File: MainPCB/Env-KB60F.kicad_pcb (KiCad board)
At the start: 2 copper layers, 283 x 126.5 mm, 143 parts, among them SW1 EVQ-P7A01P, U1 Pico

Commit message: Moved MCU lower to allow for mount hole to fit properly, Generated Gerber and bottom plate Gerber
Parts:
- moved 5.1K1 9.31 mm to (297.2, 37.0), turned to 180 degrees
- moved 5.1K2 5.92 mm to (297.2, 38.0), turned to 0 degrees
- moved U1 2.75 mm to (334.0, 51.8)
- moved H11 1.75 mm to (353.1, 36.5)
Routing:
- net col0: track 358.9 -> 350.4 mm
- net Net-(5.1K1-Pad1): track 1.71 -> 9.36 mm
- net col1: track 328.2 -> 320.6 mm
- net GND: track 10.6 -> 3.23 mm
- net VBUS: track 78.3 -> 85.7 mm, vias 0 -> 2
- net row0: track 245.8 -> 240.7 mm
- net col2: track 298.7 -> 293.9 mm
- net USB2_P: track 65.2 -> 69.8 mm, vias 1 -> 3
- net USB2_N: track 61.5 -> 66.1 mm, vias 1 -> 2
- net col14: track 142.9 -> 138.5 mm
- net Net-(5.1K2-Pad2): track 1.40 -> 5.80 mm
- net RUNPIN: track 39.0 -> 34.7 mm
- net col3: track 305.6 -> 301.9 mm
- net col5: track 251.1 -> 247.5 mm
- net col4: track 264.2 -> 260.6 mm
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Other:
- net class DIFF removed
- net class USB added: clearance 0.2, trace_width 0.25, via_dia 0.8, via_drill 0.4

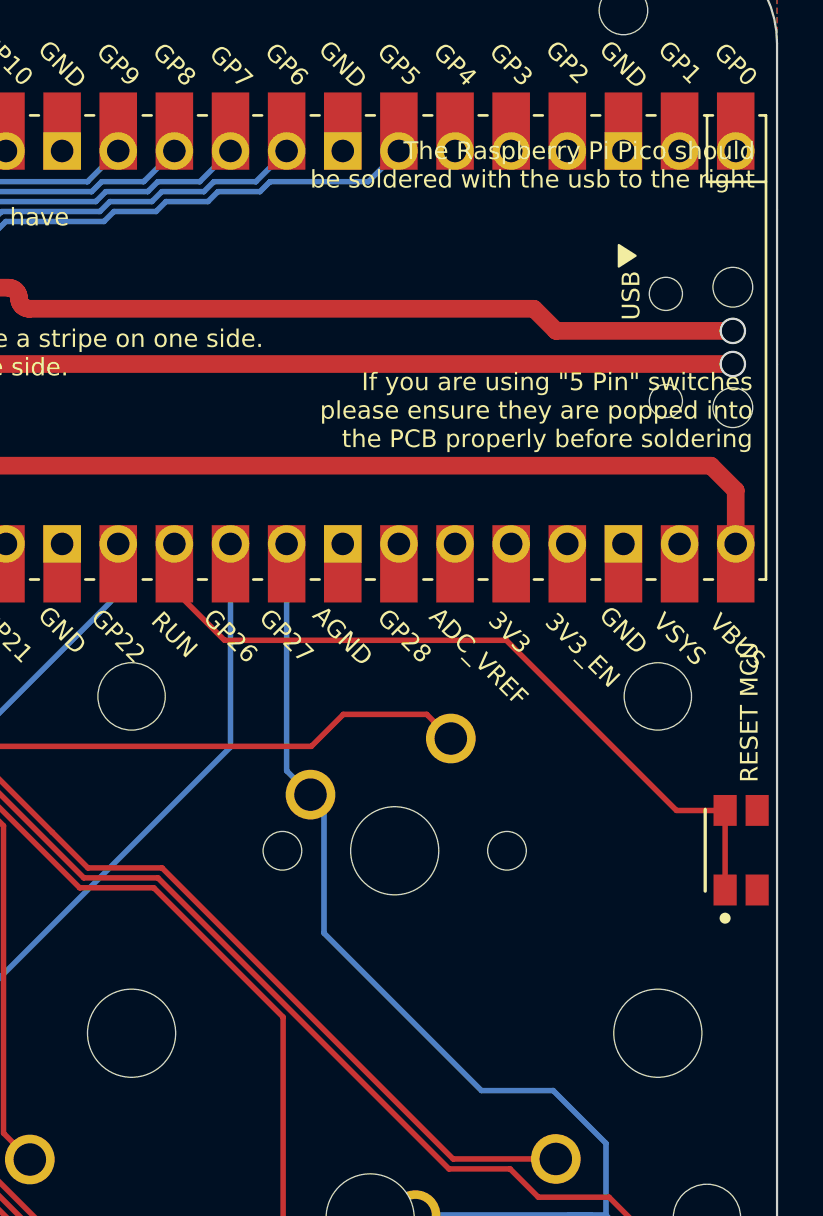
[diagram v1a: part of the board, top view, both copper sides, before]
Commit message: Corrected silkscreen, Generated updated Gerbers
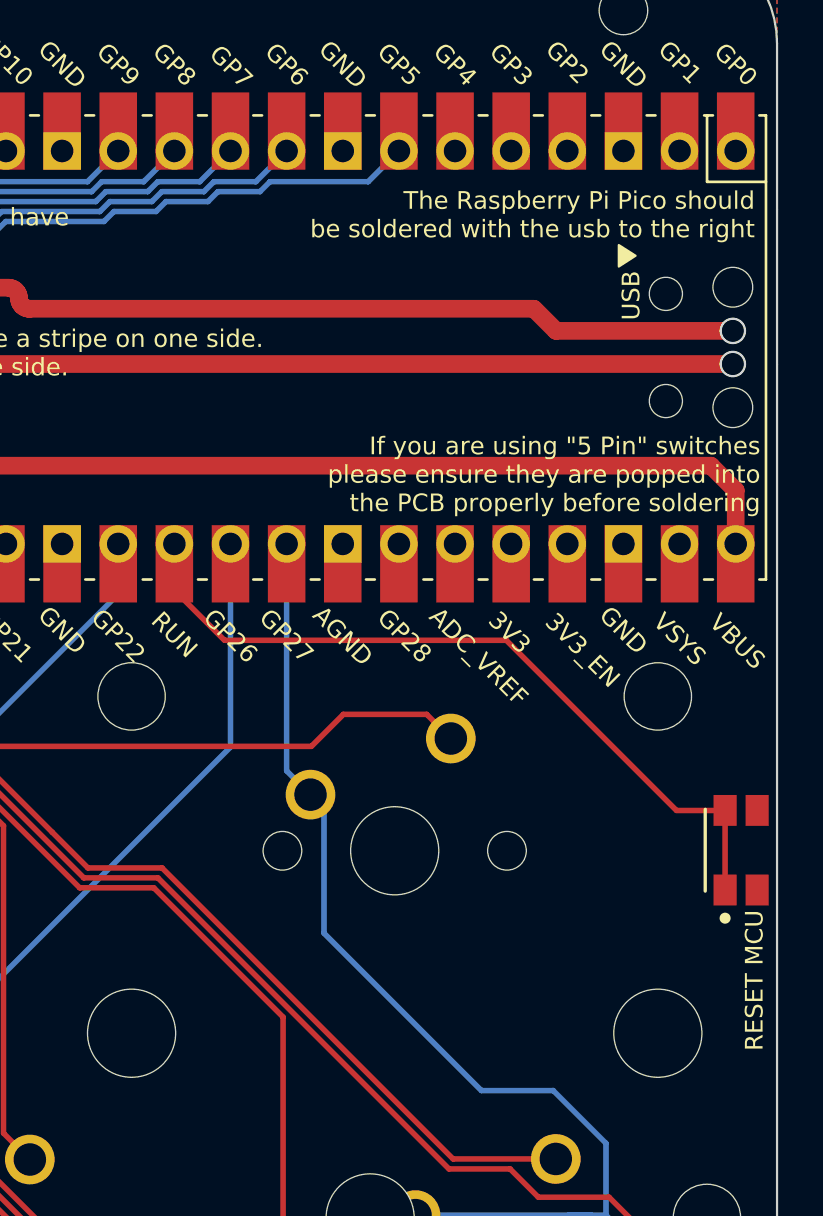
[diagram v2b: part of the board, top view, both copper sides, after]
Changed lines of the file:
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@@
     (pcbplotparams
       (layerselection 0x010fc_ffffffff)
-      (usegerberextensions false)
+      (usegerberextensions true)
       (usegerberattributes false)
       (usegerberadvancedattributes false)
@@
       (plotinvisibletext false)
       (padsonsilk false)
-      (subtractmaskfromsilk false)
+      (subtractmaskfromsilk true)
       (outputformat 1)
       (mirror false)
@@
     (effects (font (size 1 1) (thickness 0.15)) (justify mirror))
   )
-  (gr_text "RESET MCU" (at 358.75 68.25 90) (layer F.SilkS)
-    (effects (font (size 0.8 0.8) (thickness 0.153)))
+  (gr_text "RESET MCU" (at 358.975 77.2 90) (layer F.SilkS)
+    (effects (font (size 0.8 0.8) (thickness 0.153)) (justify right))
   )
   (gr_text Env-KB60F (at 85.9 56.5) (layer F.SilkS)
@@
     (effects (font (size 0.8 0.8) (thickness 0.15)))
   )
-  (gr_text "If you are using \"5 Pin\" switches\nplease ensure they are popped into\n the PCB properly before soldering" (at 358.9 54.6) (layer F.SilkS)
+  (gr_text "If you are using \"5 Pin\" switches\nplease ensure they are popped into\n the PCB properly before soldering" (at 359.25 57.5) (layer F.SilkS)
     (effects (font (size 0.8 0.8) (thickness 0.153)) (justify right))
   )
@@
     (effects (font (size 0.8 0.8) (thickness 0.153)) (justify left))
   )
-  (gr_text "The Raspberry Pi Pico should\nbe soldered with the usb to the right" (at 359 43.5) (layer F.SilkS)
+  (gr_text "The Raspberry Pi Pico should\nbe soldered with the usb to the right" (at 359 45.75) (layer F.SilkS)
     (effects (font (size 0.8 0.8) (thickness 0.153)) (justify right))
   )
@@
   (via (at 312.5 51.75) (size 0.8) (drill 0.4) (layers F.Cu B.Cu) (net 96))
   (via (at 306.3 62) (size 0.8) (drill 0.4) (layers F.Cu B.Cu) (net 96))
-  (via (at 300.75 42.6) (size 0.8) (drill 0.4) (layers F.Cu B.Cu) (net 100))
-  (via (at 358 51) (size 1.2) (drill 1) (layers F.Cu B.Cu) (net 103))
-  (via (at 358 52.5) (size 1.2) (drill 1) (layers F.Cu B.Cu) (net 104))
   (segment (start 357.65 76.3) (end 357.65 72.7) (width 0.25) (layer F.Cu) (net 97))
   (segment (start 347.75 65) (end 335 65) (width 0.25) (layer F.Cu) (net 97))
@@
   (segment (start 289.7 43.3) (end 291.38 43.3) (width 0.25) (layer F.Cu) (net 99))
   (segment (start 287.2 45.8) (end 289.7 43.3) (width 0.25) (layer F.Cu) (net 99))
+  (via (at 300.75 42.6) (size 0.8) (drill 0.4) (layers F.Cu B.Cu) (net 100))
   (via (at 307.3 43.25) (size 0.8) (drill 0.4) (layers F.Cu B.Cu) (net 100))
   (segment (start 305.445001 41.625001) (end 307.07 43.25) (width 0.5) (layer F.Cu) (net 100))
@@
   (segment (start 304.245001 38.645001) (end 302.6 37) (width 0.25) (layer F.Cu) (net 102))
   (segment (start 304.245001 40.650001) (end 304.245001 38.645001) (width 0.25) (layer F.Cu) (net 102))
+  (via (at 358 51) (size 1.2) (drill 1) (layers F.Cu B.Cu) (net 103))
   (segment (start 302.745001 41.995001) (end 303.75 43) (width 0.25) (layer F.Cu) (net 103))
   (segment (start 302.745001 40.650001) (end 302.745001 41.995001) (width 0.25) (layer F.Cu) (net 103))
@@
   (segment (start 323.972821 50.774173) (end 324.029633 50.683758) (width 0.8) (layer F.Cu) (net 103))
   (segment (start 324.076857 50.476857) (end 324.076857 50) (width 0.8) (layer F.Cu) (net 103))
+  (via (at 358 52.5) (size 1.2) (drill 1) (layers F.Cu B.Cu) (net 104))
   (segment (start 303.245001 39.177501) (end 303.245001 40.650001) (width 0.25) (layer F.Cu) (net 104))
   (segment (start 302.7675 38.7) (end 303.245001 39.177501) (width 0.25) (layer F.Cu) (net 104))

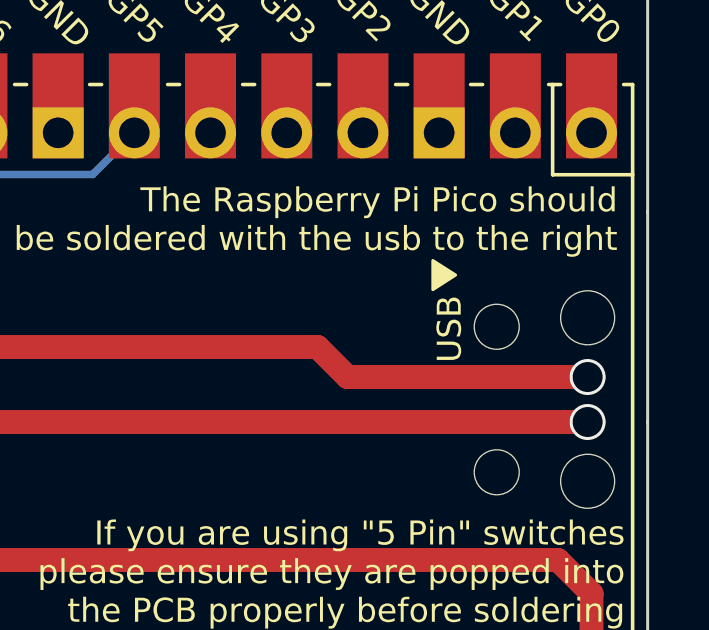
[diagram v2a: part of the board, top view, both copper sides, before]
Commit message: somehow missed a screwup on the silkscreen
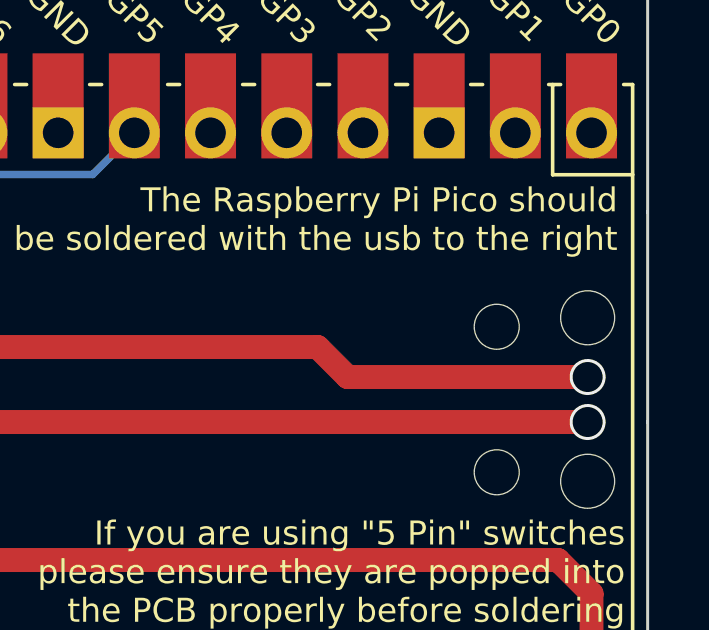
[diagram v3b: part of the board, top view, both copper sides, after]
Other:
- board text removed: "USB"

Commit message: General Checkover and adjustments, Generated Gerbers for JLCPCB
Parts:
- added J1: TP3 Pad, TestPoint:TestPoint_Pad_1.0x1.0mm, F.Cu at (358.0, 51.0)
- added J2: TP2 Pad, TestPoint:TestPoint_Pad_1.0x1.0mm, F.Cu at (358.0, 52.6)
- 5.1K1, 5.1K2: value R_Small -> 5.1K 0402 Resistor; footprint Resistor_SMD:R_0201_0603Metric -> Resistor_SMD:R_0402_1005Metric
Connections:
- USB1 pad 3: (no net) -> Net-(USB1-Pad3)
- USB1 pad 9: (no net) -> Net-(USB1-Pad9)

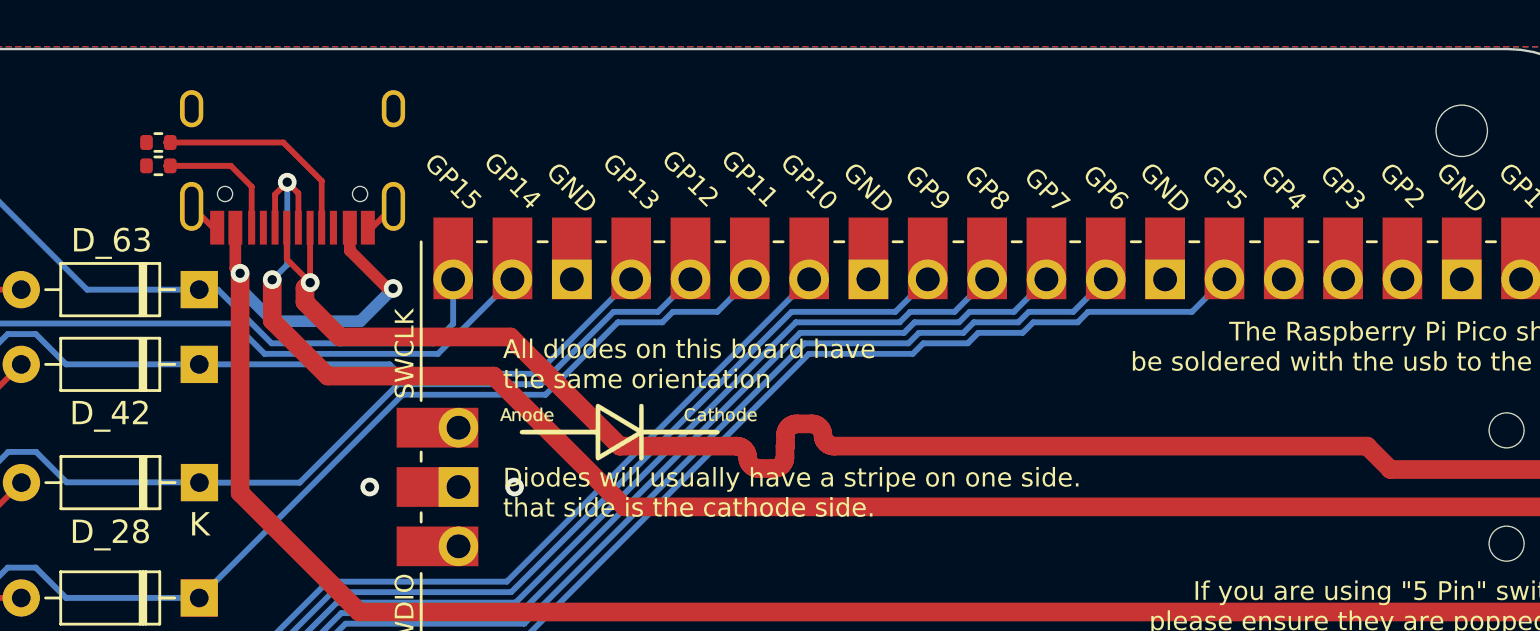
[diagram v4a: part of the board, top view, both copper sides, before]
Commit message: Tweaked USB P/N Traces
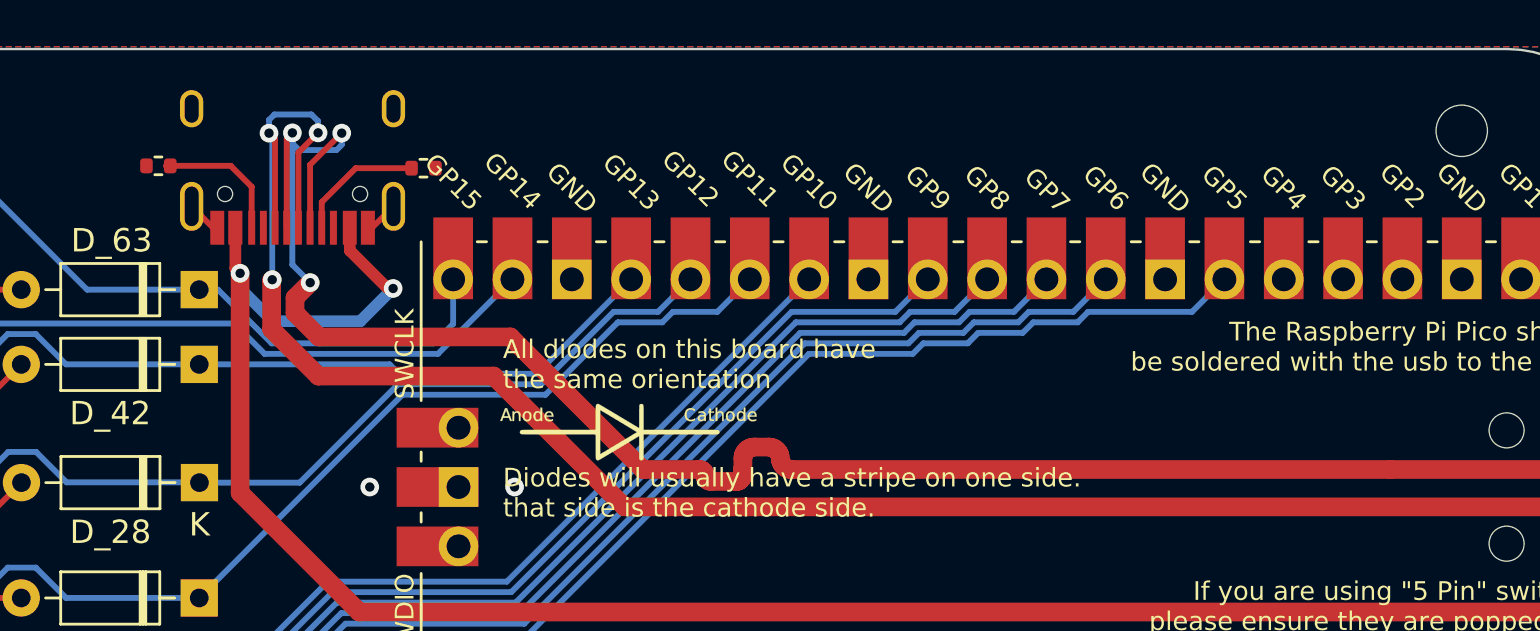
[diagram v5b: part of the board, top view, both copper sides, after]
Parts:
- moved 5.1K1 11.4 mm to (308.6, 38.1), turned to 0 degrees
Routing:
- net USB2_N: track 66.1 -> 80.0 mm, vias 2 -> 4
- net USB2_P: track 69.9 -> 79.6 mm, vias 3 -> 4
- net Net-(5.1K1-Pad1): track 9.36 -> 5.54 mm

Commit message: Generated DXF for CNC or Laser cut.
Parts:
- H1, H10, H11, H2, H3, H4, H6, H9: footprint MountingHole:MountingHole_2.2mm_M2 -> AKLogo:MountingHole_2.2mm_M2-MODIFIED

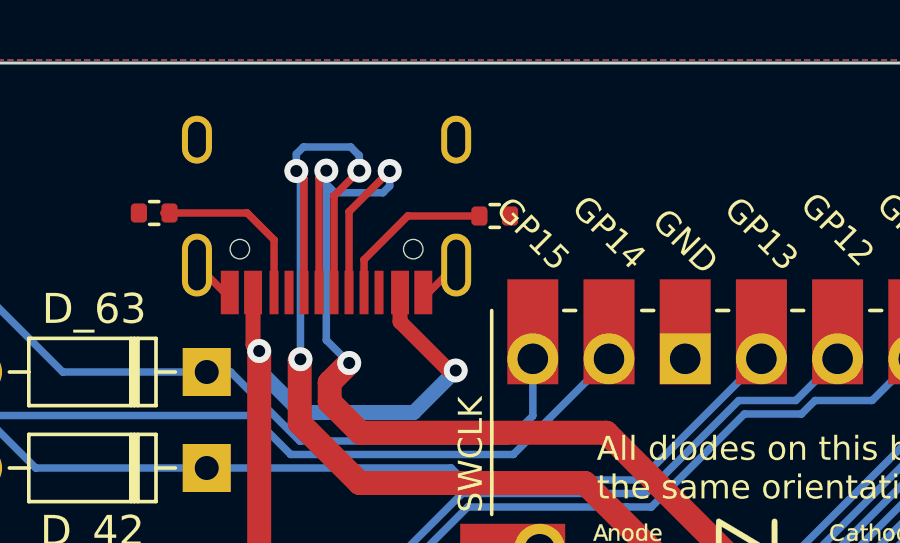
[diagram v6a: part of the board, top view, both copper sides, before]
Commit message: moved a CC resistor out of the way of some silkscreen.
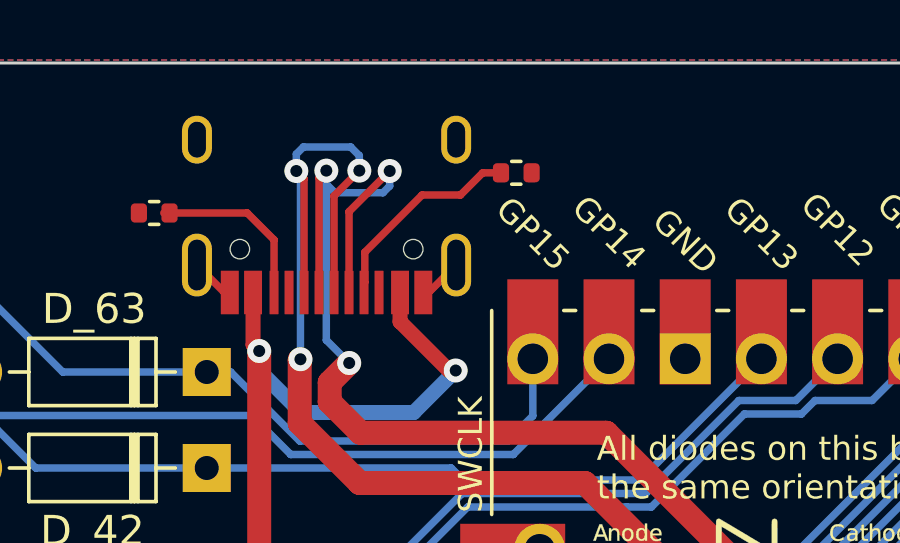
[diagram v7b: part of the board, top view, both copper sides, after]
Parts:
- moved 5.1K1 1.61 mm to (309.3, 36.7)
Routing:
- net Net-(5.1K1-Pad1): track 5.54 -> 6.99 mm
